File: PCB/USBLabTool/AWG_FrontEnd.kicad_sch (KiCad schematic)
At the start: 36 parts, among them J17 2x01, J18 02x02, U1 Opamp_Quad, U10 Opamp_Quad, U11 DG403, U2 Opamp_Quad, U3 DG403, U9 Opamp_Quad

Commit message: add Logic Analyzer and finish pins
Add Logic Analyzer. Add separate pins to 20 pins input(logic and scope) and 4 pins output(AWG). Add 4 programing pins.
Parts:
- removed J18: 02x02, Connector_PinHeader_2.54mm:PinHeader_2x02_P2.54mm_Vertical, symbol Connector_Generic:Conn_02x02_Counter_Clockwise
- added J2: 02x02, awg_fp_lib:2x02, symbol Connector_Generic:Conn_02x02_Counter_Clockwise
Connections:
- net GND: now also J2.3 (Pin_3), J2.4 (Pin_4)
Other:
- note removed: "Will change this later on when connect them to a 20 pins"
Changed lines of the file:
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@@
 	)
 	(junction
+		(at 224.79 80.01)
+		(diameter 0)
+		(color 0 0 0 0)
+	)
+	(junction
 		(at 78.74 86.36)
 		(diameter 0)
@@
 	)
 	(junction
-		(at 210.82 86.36)
-		(diameter 0)
-		(color 0 0 0 0)
-	)
-	(junction
 		(at 147.32 114.3)
 		(diameter 0)
@@
 	(wire
 		(pts
-			(xy 198.12 55.88) (xy 198.12 83.82)
-		)
-		(stroke
-			(width 0)
-			(type default)
-		)
-	)
-	(wire
-		(pts
 			(xy 48.26 55.88) (xy 58.42 55.88)
 		)
@@
 	(wire
 		(pts
-			(xy 210.82 86.36) (xy 210.82 83.82)
-		)
-		(stroke
-			(width 0)
-			(type default)
-		)
-	)
-	(wire
-		(pts
 			(xy 147.32 50.8) (xy 147.32 55.88)
 		)
@@
 	(wire
 		(pts
-			(xy 198.12 86.36) (xy 198.12 114.3)
+			(xy 198.12 87.63) (xy 198.12 114.3)
 		)
 		(stroke
@@
 	(wire
 		(pts
+			(xy 198.12 55.88) (xy 198.12 69.85)
+		)
+		(stroke
+			(width 0)
+			(type default)
+		)
+	)
+	(wire
+		(pts
 			(xy 167.64 111.76) (xy 154.94 111.76)
 		)
@@
 	(wire
 		(pts
+			(xy 224.79 80.01) (xy 224.79 77.47)
+		)
+		(stroke
+			(width 0)
+			(type default)
+		)
+	)
+	(wire
+		(pts
 			(xy 58.42 45.72) (xy 63.5 45.72)
 		)
@@
 		)
 	)
-	(text "Will change this later on when connect them to a 20 pins\n"
-		(exclude_from_sim no)
-		(at 226.822 71.882 0)
-		(effects
-			(font
-				(size 1.27 1.27)
-			)
-		)
-	)
 	(text "AWG CHAN 0"
 		(exclude_from_sim no)
@@
 	(label "C0_OUT_G"
 		(at 111.76 55.88 0)
+		(fields_autoplaced yes)
 		(effects
 			(font
@@
 	(label "C0_V_OFF"
 		(at 88.9 27.94 180)
+		(fields_autoplaced yes)
 		(effects
 			(font
@@
 	(label "C1_V_OFF"
 		(at 96.52 86.36 180)
+		(fields_autoplaced yes)
 		(effects
 			(font
@@
 	(label "C1_OUT_GO"
 		(at 195.58 114.3 180)
+		(fields_autoplaced yes)
 		(effects
 			(font
@@
 	(label "C0_OUT_GO"
 		(at 195.58 55.88 180)
+		(fields_autoplaced yes)
 		(effects
 			(font
@@
 	(label "C1_IN"
 		(at 48.26 114.3 0)
+		(fields_autoplaced yes)
 		(effects
 			(font
@@
 	(label "C1_FB"
 		(at 96.52 104.14 0)
+		(fields_autoplaced yes)
 		(effects
 			(font
@@
 	(label "C1_OUT_G"
 		(at 111.76 114.3 0)
+		(fields_autoplaced yes)
 		(effects
 			(font
@@
 	(label "C0_IN"
 		(at 48.26 55.88 0)
+		(fields_autoplaced yes)
 		(effects
 			(font
@@
 	(label "C0_FB"
 		(at 96.52 45.72 0)
+		(fields_autoplaced yes)
 		(effects
 			(font
@@
 	(global_label "DAC1_OUT1"
 		(shape input)
-		(at 198.12 76.2 0)
+		(at 198.12 69.85 0)
 		(fields_autoplaced yes)
 		(effects
@@
 		)
 		(property "Intersheetrefs" "${INTERSHEET_REFS}"
-			(at 211.749 76.2 0)
+			(at 211.749 69.85 0)
 			(effects
 				(font
@@
 	(global_label "DAC1_OUT2"
 		(shape input)
-		(at 198.12 93.98 0)
+		(at 198.12 87.63 0)
 		(fields_autoplaced yes)
 		(effects
@@
 		)
 		(property "Intersheetrefs" "${INTERSHEET_REFS}"
-			(at 211.749 93.98 0)
+			(at 211.749 87.63 0)
 			(effects
 				(font
@@
 	)
 	(symbol
-		(lib_name "GND_1")
-		(lib_id "power:GND")
-		(at 210.82 86.36 0)
+		(lib_id "power:GNDA")
+		(at 55.88 38.1 0)
 		(unit 1)
 		(exclude_from_sim no)
@@
 		(on_board yes)
 		(dnp no)
-		(property "Reference" "#PWR065"
-			(at 210.82 92.71 0)
+		(fields_autoplaced yes)
+		(property "Reference" "#PWR055"
+			(at 55.88 44.45 0)
 			(effects
 				(font
@@
 		)
 		(property "Value" "GNDA"
-			(at 213.36 90.424 0)
+			(at 55.88 43.18 0)
 			(effects
 				(font
 					(size 1.27 1.27)
 				)
-				(justify right)
 			)
 		)
 		(property "Footprint" ""
-			(at 210.82 86.36 0)
+			(at 55.88 38.1 0)
 			(effects
 				(font
@@
 		)
 		(property "Datasheet" ""
-			(at 210.82 86.36 0)
+			(at 55.88 38.1 0)
 			(effects
 				(font
@@
 		)
 		(property "Description" ""
-			(at 210.82 86.36 0)
+			(at 55.88 38.1 0)
 			(effects
 				(font
@@
 		)
 		(instances
-			(project ""
-				(path "/ac21a78e-8237-4dbe-925d-fc53d85eb1b9"
-					(reference "#PWR065")
-					(unit 1)
-				)
-			)
 			(project "USBLabTool"
 				(path "/b5440f7d-90d5-417e-adc2-aa6b11e5424d/51eab4b3-0b2f-418c-9f7c-59af443ff2ad"
-					(reference "#PWR067")
+					(reference "#PWR055")
 					(unit 1)
 				)
@@
 	)
 	(symbol
-		(lib_id "power:GNDA")
-		(at 55.88 38.1 0)
+		(lib_id "power:GND")
+		(at 224.79 80.01 0)
 		(unit 1)
 		(exclude_from_sim no)
@@
 		(on_board yes)
 		(dnp no)
-		(fields_autoplaced yes)
-		(property "Reference" "#PWR055"
-			(at 55.88 44.45 0)
+		(property "Reference" "#PWR0157"
+			(at 224.79 86.36 0)
 			(effects
 				(font
@@
 			)
 		)
-		(property "Value" "GNDA"
-			(at 55.88 43.18 0)
+		(property "Value" "GND"
+			(at 226.568 84.074 0)
 			(effects
 				(font
 					(size 1.27 1.27)
 				)
+				(justify right)
 			)
 		)
 		(property "Footprint" ""
-			(at 55.88 38.1 0)
+			(at 224.79 80.01 0)
 			(effects
 				(font
@@
 		)
 		(property "Datasheet" ""
-			(at 55.88 38.1 0)
+			(at 224.79 80.01 0)
 			(effects
 				(font
@@
 		)
 		(property "Description" ""
-			(at 55.88 38.1 0)
+			(at 224.79 80.01 0)
 			(effects
 				(font
@@
 			(project "USBLabTool"
 				(path "/b5440f7d-90d5-417e-adc2-aa6b11e5424d/51eab4b3-0b2f-418c-9f7c-59af443ff2ad"
-					(reference "#PWR055")
+					(reference "#PWR0157")
 					(unit 1)
 				)
@@
 	)
 	(symbol
-		(lib_id "Device:R")
-		(at 151.13 114.3 90)
+		(lib_id "Connector_Generic:Conn_02x02_Counter_Clockwise")
+		(at 217.17 77.47 0)
 		(unit 1)
 		(exclude_from_sim no)
@@
 		(on_board yes)
 		(dnp no)
-		(property "Reference" "R46"
-			(at 151.13 111.76 90)
+		(property "Reference" "J2"
+			(at 218.44 74.168 0)
 			(effects
 				(font
@@
 			)
 		)
-		(property "Value" "10K"
-			(at 151.13 114.3 90)
+		(property "Value" "02x02"
+			(at 218.44 74.168 0)
 			(effects
 				(font
 					(size 1.27 1.27)
 				)
+				(hide yes)
 			)
 		)
-		(property "Footprint" "Resistor_SMD:R_0603_1608Metric"
-			(at 151.13 116.078 90)
+		(property "Footprint" "awg_fp_lib:2x02"
+			(at 217.17 77.47 0)
 			(effects
 				(font
@@
 		)
 		(property "Datasheet" "~"
-			(at 151.13 114.3 0)
+			(at 217.17 77.47 0)
 			(effects
 				(font
@@
 		)
 		(property "Description" ""
-			(at 151.13 114.3 0)
+			(at 217.17 77.47 0)
 			(effects
 				(font
@@
 		(pin "2"
 		)
+		(pin "3"
+		)
+		(pin "4"
+		)
 		(instances
 			(project "USBLabTool"
 				(path "/b5440f7d-90d5-417e-adc2-aa6b11e5424d/51eab4b3-0b2f-418c-9f7c-59af443ff2ad"
-					(reference "R46")
+					(reference "J2")
 					(unit 1)
 				)
@@
 	)
 	(symbol
-		(lib_id "Connector_Generic:Conn_02x02_Counter_Clockwise")
-		(at 203.2 83.82 0)
+		(lib_id "Device:R")
+		(at 151.13 114.3 90)
 		(unit 1)
 		(exclude_from_sim no)
@@
 		(on_board yes)
 		(dnp no)
-		(property "Reference" "J18"
-			(at 204.47 80.518 0)
+		(property "Reference" "R46"
+			(at 151.13 111.76 90)
 			(effects
 				(font
@@
 			)
 		)
-		(property "Value" "02x02"
-			(at 204.47 80.518 0)
+		(property "Value" "10K"
+			(at 151.13 114.3 90)
 			(effects
 				(font
 					(size 1.27 1.27)
 				)
-				(hide yes)
 			)
 		)
-		(property "Footprint" "Connector_PinHeader_2.54mm:PinHeader_2x02_P2.54mm_Vertical"
-			(at 203.2 83.82 0)
+		(property "Footprint" "Resistor_SMD:R_0603_1608Metric"
+			(at 151.13 116.078 90)
 			(effects
 				(font
@@
 		)
 		(property "Datasheet" "~"
-			(at 203.2 83.82 0)
+			(at 151.13 114.3 0)
 			(effects
 				(font
@@
 		)
 		(property "Description" ""
-			(at 203.2 83.82 0)
+			(at 151.13 114.3 0)
 			(effects
 				(font
@@
 		(pin "2"
 		)
-		(pin "3"
-		)
-		(pin "4"
-		)
 		(instances
 			(project "USBLabTool"
 				(path "/b5440f7d-90d5-417e-adc2-aa6b11e5424d/51eab4b3-0b2f-418c-9f7c-59af443ff2ad"
-					(reference "J18")
+					(reference "R46")
 					(unit 1)
 				)

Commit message: minor fixes
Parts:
- removed J2: 02x02, awg_fp_lib:2x02, symbol Connector_Generic:Conn_02x02_Counter_Clockwise
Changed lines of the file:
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@@
 	)
 	(junction
-		(at 224.79 80.01)
-		(diameter 0)
-		(color 0 0 0 0)
-	)
-	(junction
 		(at 78.74 86.36)
 		(diameter 0)
@@
 	(wire
 		(pts
-			(xy 224.79 80.01) (xy 224.79 77.47)
-		)
-		(stroke
-			(width 0)
-			(type default)
-		)
-	)
-	(wire
-		(pts
 			(xy 58.42 45.72) (xy 63.5 45.72)
 		)
@@
 	)
 	(symbol
-		(lib_id "power:GND")
-		(at 224.79 80.01 0)
-		(unit 1)
-		(exclude_from_sim no)
-		(in_bom yes)
-		(on_board yes)
-		(dnp no)
-		(property "Reference" "#PWR0157"
-			(at 224.79 86.36 0)
-			(effects
-				(font
-					(size 1.27 1.27)
-				)
-				(hide yes)
-			)
-		)
-		(property "Value" "GND"
-			(at 226.568 84.074 0)
-			(effects
-				(font
-					(size 1.27 1.27)
-				)
-				(justify right)
-			)
-		)
-		(property "Footprint" ""
-			(at 224.79 80.01 0)
-			(effects
-				(font
-					(size 1.27 1.27)
-				)
-				(hide yes)
-			)
-		)
-		(property "Datasheet" ""
-			(at 224.79 80.01 0)
-			(effects
-				(font
-					(size 1.27 1.27)
-				)
-				(hide yes)
-			)
-		)
-		(property "Description" ""
-			(at 224.79 80.01 0)
-			(effects
-				(font
-					(size 1.27 1.27)
-				)
-				(hide yes)
-			)
-		)
-		(pin "1"
-		)
-		(instances
-			(project "USBLabTool"
-				(path "/b5440f7d-90d5-417e-adc2-aa6b11e5424d/51eab4b3-0b2f-418c-9f7c-59af443ff2ad"
-					(reference "#PWR0157")
-					(unit 1)
-				)
-			)
-		)
-	)
-	(symbol
 		(lib_id "Device:R")
 		(at 55.88 24.13 0)
@@
 					(unit 1)
 				)
-			)
-		)
-	)
-	(symbol
-		(lib_id "Connector_Generic:Conn_02x02_Counter_Clockwise")
-		(at 217.17 77.47 0)
-		(unit 1)
-		(exclude_from_sim no)
-		(in_bom yes)
-		(on_board yes)
-		(dnp no)
-		(property "Reference" "J2"
-			(at 218.44 74.168 0)
-			(effects
-				(font
-					(size 1.27 1.27)
-				)
-			)
-		)
-		(property "Value" "02x02"
-			(at 218.44 74.168 0)
-			(effects
-				(font
-					(size 1.27 1.27)
-				)
-				(hide yes)
-			)
-		)
-		(property "Footprint" "awg_fp_lib:2x02"
-			(at 217.17 77.47 0)
-			(effects
-				(font
-					(size 1.27 1.27)
-				)
-				(hide yes)
-			)
-		)
-		(property "Datasheet" "~"
-			(at 217.17 77.47 0)
-			(effects
-				(font
-					(size 1.27 1.27)
-				)
-				(hide yes)
-			)
-		)
-		(property "Description" ""
-			(at 217.17 77.47 0)
-			(effects
-				(font
-					(size 1.27 1.27)
-				)
-				(hide yes)
-			)
-		)
-		(pin "1"
-		)
-		(pin "2"
-		)
-		(pin "3"
-		)
-		(pin "4"
-		)
-		(instances
-			(project "USBLabTool"
-				(path "/b5440f7d-90d5-417e-adc2-aa6b11e5424d/51eab4b3-0b2f-418c-9f7c-59af443ff2ad"
-					(reference "J2")
-					(unit 1)
-				)

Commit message: continue PCB layout
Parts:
- renumbered R6 to R33, R3 to R34, R4 to R35, R5 to R43, R1 to R50, R2 to R52, U1 to U10, U2 to U10, U3 to U11, U1 to U9
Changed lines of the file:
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@@
 (kicad_sch
-	(version 20231120)
+	(version 20250114)
 	(generator "eeschema")
-	(generator_version "8.0")
+	(generator_version "9.0")
 	(paper "A4")
+	(text "AWG CHAN 0"
+		(exclude_from_sim no)
+		(at 13.462 29.718 0)
+		(effects
+			(font
+				(size 3.81 3.81)
+			)
+			(justify left bottom)
+		)
+	)
+	(text "AWG CHAN 1"
+		(exclude_from_sim no)
+		(at 13.97 67.818 0)
+		(effects
+			(font
+				(size 3.81 3.81)
+			)
+			(justify left bottom)
+		)
+	)
+	(text "5K/10K"
+		(exclude_from_sim no)
+		(at 154.94 119.38 0)
+		(effects
+			(font
+				(size 1.27 1.27)
+			)
+			(justify right bottom)
+		)
+	)
+	(text "Switch U12A and U12B do not connect to U12C power source but KiCad will give false warnings if names are changed. DO NOT CONNECT THEM TOGETHER!!"
+		(exclude_from_sim no)
+		(at 14.986 152.654 0)
+		(effects
+			(font
+				(size 1.27 1.27)
+			)
+			(justify left)
+		)
+	)
+	(text "5K/10K"
+		(exclude_from_sim no)
+		(at 156.21 60.96 0)
+		(effects
+			(font
+				(size 1.27 1.27)
+			)
+			(justify right bottom)
+		)
+	)
 	(junction
 		(at 137.16 55.88)
@@
 		)
 	)
-	(text "AWG CHAN 0"
-		(exclude_from_sim no)
-		(at 13.462 29.718 0)
-		(effects
-			(font
-				(size 3.81 3.81)
-			)
-			(justify left bottom)
-		)
-	)
-	(text "AWG CHAN 1"
-		(exclude_from_sim no)
-		(at 13.97 67.818 0)
-		(effects
-			(font
-				(size 3.81 3.81)
-			)
-			(justify left bottom)
-		)
-	)
-	(text "5K/10K"
-		(exclude_from_sim no)
-		(at 154.94 119.38 0)
-		(effects
-			(font
-				(size 1.27 1.27)
-			)
-			(justify right bottom)
-		)
-	)
-	(text "Switch U12A and U12B do not connect to U12C power source but KiCad will give false warnings if names are changed. DO NOT CONNECT THEM TOGETHER!!"
-		(exclude_from_sim no)
-		(at 14.986 152.654 0)
-		(effects
-			(font
-				(size 1.27 1.27)
-			)
-			(justify left)
-		)
-	)
-	(text "5K/10K"
-		(exclude_from_sim no)
-		(at 156.21 60.96 0)
-		(effects
-			(font
-				(size 1.27 1.27)
-			)
-			(justify right bottom)
-		)
-	)
 	(label "C0_OUT_G"
 		(at 111.76 55.88 0)
@@
 		(on_board yes)
 		(dnp no)
-		(property "Reference" "#PWR048"
+		(property "Reference" "#PWR056"
 			(at 55.88 102.87 0)
 			(effects
@@
 		(dnp no)
 		(fields_autoplaced yes)
-		(property "Reference" "U1"
+		(property "Reference" "U10"
 			(at 71.12 102.87 0)
 			(effects
@@
 		(dnp no)
 		(fields_autoplaced yes)
-		(property "Reference" "U1"
+		(property "Reference" "U9"
 			(at 71.12 43.18 0)
 			(effects
@@
 		(dnp no)
 		(fields_autoplaced yes)
-		(property "Reference" "U3"
+		(property "Reference" "U11"
 			(at 119.38 91.44 0)
 			(effects
@@
 		(on_board yes)
 		(dnp no)
-		(property "Reference" "R3"
+		(property "Reference" "R34"
 			(at 58.42 82.55 90)
 			(effects
@@
 		(dnp no)
 		(fields_autoplaced yes)
-		(property "Reference" "U2"
+		(property "Reference" "U10"
 			(at 175.26 104.14 0)
 			(effects
@@
 		(on_board yes)
 		(dnp no)
-		(property "Reference" "R6"
+		(property "Reference" "R33"
 			(at 58.42 24.13 90)
 			(effects
@@
 		(on_board yes)
 		(dnp no)
-		(property "Reference" "R1"
+		(property "Reference" "R50"
 			(at 158.75 104.14 90)
 			(effects
@@
 		(on_board yes)
 		(dnp no)
-		(property "Reference" "#PWR063"
+		(property "Reference" "#PWR066"
 			(at 185.42 31.75 0)
 			(effects
@@
 		(on_board yes)
 		(dnp no)
-		(property "Reference" "R5"
+		(property "Reference" "R43"
 			(at 151.13 48.26 90)
 			(effects
@@
 		(on_board yes)
 		(dnp no)
-		(property "Reference" "R4"
+		(property "Reference" "R35"
 			(at 90.17 43.18 90)
 			(effects
@@
 		(on_board yes)
 		(dnp no)
-		(property "Reference" "U1"
+		(property "Reference" "U9"
 			(at 106.68 66.04 0)
 			(effects
@@
 		(on_board yes)
 		(dnp no)
-		(property "Reference" "#PWR062"
+		(property "Reference" "#PWR065"
 			(at 172.72 33.02 0)
 			(effects
@@
 		(on_board yes)
 		(dnp no)
-		(property "Reference" "R2"
+		(property "Reference" "R52"
 			(at 176.53 99.06 90)
 			(effects
@@
 		)
 	)
+	(embedded_fonts no)
 )

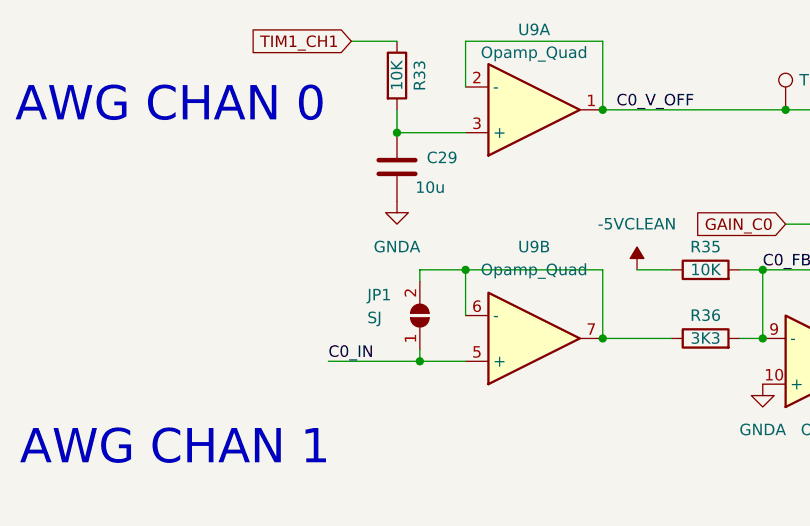
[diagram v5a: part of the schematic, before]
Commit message: fixed grounds for several components and fix 5V clean
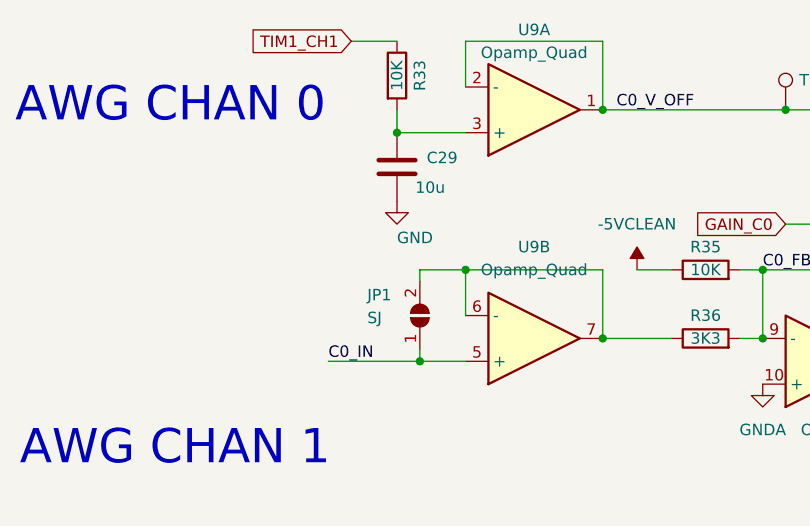
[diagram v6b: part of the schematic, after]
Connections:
- net GND: now also C29.2
- net GNDA: no longer C29.2
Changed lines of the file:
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@@
 		(on_board yes)
 		(dnp no)
-		(fields_autoplaced yes)
 		(property "Reference" "#PWR055"
 			(at 55.88 44.45 0)
@@
 			)
 		)
-		(property "Value" "GNDA"
-			(at 55.88 43.18 0)
+		(property "Value" "GND"
+			(at 55.88 42.164 0)
 			(effects
 				(font
 					(size 1.27 1.27)
 				)
+				(justify left)
 			)
 		)

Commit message: fix footprint and change button
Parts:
- U10, U9: footprint Package_SO:SOIC-14W_7.5x9mm_P1.27mm -> Package_SO:SOIC-14_3.9x8.7mm_P1.27mm
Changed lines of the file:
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@@
 			)
 		)
-		(property "Footprint" "Package_SO:SOIC-14W_7.5x9mm_P1.27mm"
+		(property "Footprint" "Package_SO:SOIC-14_3.9x8.7mm_P1.27mm"
 			(at 71.12 111.76 0)
 			(effects
@@
 			)
 		)
+		(property "Purpose" ""
+			(at 71.12 111.76 0)
+			(effects
+				(font
+					(size 1.27 1.27)
+				)
+				(hide yes)
+			)
+		)
 		(pin "1"
 		)
@@
 			)
 		)
-		(property "Footprint" "Package_SO:SOIC-14W_7.5x9mm_P1.27mm"
+		(property "Footprint" "Package_SO:SOIC-14_3.9x8.7mm_P1.27mm"
 			(at 71.12 53.34 0)
 			(effects
@@
 			)
 		)
+		(property "Purpose" ""
+			(at 71.12 53.34 0)
+			(effects
+				(font
+					(size 1.27 1.27)
+				)
+				(hide yes)
+			)
+		)
 		(pin "1"
 		)
@@
 			)
 		)
-		(property "Footprint" "Package_SO:SOIC-14W_7.5x9mm_P1.27mm"
+		(property "Footprint" "Package_SO:SOIC-14_3.9x8.7mm_P1.27mm"
 			(at 71.12 86.36 0)
 			(effects
@@
 			)
 		)
+		(property "Purpose" ""
+			(at 71.12 86.36 0)
+			(effects
+				(font
+					(size 1.27 1.27)
+				)
+				(hide yes)
+			)
+		)
 		(pin "1"
 		)
@@
 			)
 		)
-		(property "Footprint" "Package_SO:SOIC-14W_7.5x9mm_P1.27mm"
+		(property "Footprint" "Package_SO:SOIC-14_3.9x8.7mm_P1.27mm"
 			(at 175.26 114.3 0)
 			(effects
@@
 			)
 		)
+		(property "Purpose" ""
+			(at 175.26 114.3 0)
+			(effects
+				(font
+					(size 1.27 1.27)
+				)
+				(hide yes)
+			)
+		)
 		(pin "1"
 		)
@@
 			)
 		)
-		(property "Footprint" "Package_SO:SOIC-14W_7.5x9mm_P1.27mm"
+		(property "Footprint" "Package_SO:SOIC-14_3.9x8.7mm_P1.27mm"
 			(at 175.26 55.88 0)
 			(effects
@@
 			)
 		)
+		(property "Purpose" ""
+			(at 175.26 55.88 0)
+			(effects
+				(font
+					(size 1.27 1.27)
+				)
+				(hide yes)
+			)
+		)
 		(pin "1"
 		)
@@
 			)
 		)
-		(property "Footprint" "Package_SO:SOIC-14W_7.5x9mm_P1.27mm"
+		(property "Footprint" "Package_SO:SOIC-14_3.9x8.7mm_P1.27mm"
 			(at 104.14 55.88 0)
 			(effects
@@
 			)
 		)
+		(property "Purpose" ""
+			(at 104.14 55.88 0)
+			(effects
+				(font
+					(size 1.27 1.27)
+				)
+				(hide yes)
+			)
+		)
 		(pin "1"
 		)
@@
 			)
 		)
-		(property "Footprint" "Package_SO:SOIC-14W_7.5x9mm_P1.27mm"
+		(property "Footprint" "Package_SO:SOIC-14_3.9x8.7mm_P1.27mm"
 			(at 71.12 27.94 0)
 			(effects
@@
 			)
 		)
+		(property "Purpose" ""
+			(at 71.12 27.94 0)
+			(effects
+				(font
+					(size 1.27 1.27)
+				)
+				(hide yes)
+			)
+		)
 		(pin "1"
 		)
@@
 			)
 		)
-		(property "Footprint" "Package_SO:SOIC-14W_7.5x9mm_P1.27mm"
+		(property "Footprint" "Package_SO:SOIC-14_3.9x8.7mm_P1.27mm"
 			(at 104.14 114.3 0)
 			(effects
@@
 			(at 104.14 114.3 0)
 			(effects
+				(font
+					(size 1.27 1.27)
+				)
+				(hide yes)
+			)
+		)
+		(property "Purpose" ""
+			(at 104.14 114.3 0)
+			(effects

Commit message: PCB updates from meeting 3/19
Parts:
- TP1, TP2, TP4: footprint TestPoint:TestPoint_THTPad_1.5x1.5mm_Drill0.7mm -> TestPoint:TestPoint_Pad_D2.0mm
- TP3: footprint TestPoint_THTPad_1.5x1.5mm_Drill0.7mm -> TestPoint:TestPoint_Pad_D2.0mm
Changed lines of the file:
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@@
 			)
 		)
-		(property "Footprint" "TestPoint:TestPoint_THTPad_1.5x1.5mm_Drill0.7mm"
+		(property "Footprint" "TestPoint:TestPoint_Pad_D2.0mm"
 			(at 104.14 27.94 0)
 			(effects
@@
 			)
 		)
-		(property "Footprint" "TestPoint_THTPad_1.5x1.5mm_Drill0.7mm"
+		(property "Footprint" "TestPoint:TestPoint_Pad_D2.0mm"
 			(at 142.24 45.72 0)
 			(effects
@@
 			)
 		)
-		(property "Footprint" "TestPoint:TestPoint_THTPad_1.5x1.5mm_Drill0.7mm"
+		(property "Footprint" "TestPoint:TestPoint_Pad_D2.0mm"
 			(at 142.24 104.14 0)
 			(effects
@@
 			)
 		)
-		(property "Footprint" "TestPoint:TestPoint_THTPad_1.5x1.5mm_Drill0.7mm"
+		(property "Footprint" "TestPoint:TestPoint_Pad_D2.0mm"
 			(at 104.14 86.36 0)
 			(effects
